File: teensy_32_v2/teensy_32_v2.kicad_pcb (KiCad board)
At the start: 2 copper layers, 65 x 56.5 mm, 62 parts, among them J1 277-1667-ND, J2 277-1667-ND, J3 CJ, J4 CJ, J5 CJ, J6 CJ, J7 M20-9980845, J8 M20-9970445, J9 TSW-108-07-G-T, P1 S9200-ND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

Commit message: more work on teensy shield
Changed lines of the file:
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@@
     (links 166)
     (no_connects 0)
-    (area 74.949999 59.949999 140.050001 116.550001)
+    (area 69.523819 58.652 146.962016 123.037092)
     (thickness 1.6)
     (drawings 87)
@@
   (page A4)
   (layers
-    (0 F.Cu signal hide)
+    (0 F.Cu signal)
     (31 B.Cu signal)
     (32 B.Adhes user hide)
@@
   )
   (setup
-    (last_trace_width 0.7)
+    (last_trace_width 1.2)
     (user_trace_width 0.25)
     (user_trace_width 0.45)
@@
     (pad_to_mask_clearance 0)
     (aux_axis_origin 0 0)
-    (visible_elements 7FFEBF7F)
+    (visible_elements 7FFEFF7F)
     (pcbplotparams
       (layerselection 0x010fc_80000001)
@@
   (segment (start 87.884 77.681) (end 86.319 77.681) (width 1.2) (layer F.Cu) (net 2))
   (segment (start 86.319 77.681) (end 84.2 79.8) (width 1.2) (layer F.Cu) (net 2))
-  (segment (start 107 96.8) (end 107 98.46) (width 0.7) (layer F.Cu) (net 2))
+  (segment (start 107 96.8) (end 107 98.46) (width 1.2) (layer F.Cu) (net 2))
   (segment (start 106.4 96.2) (end 107 96.8) (width 1.2) (layer F.Cu) (net 2))
   (segment (start 100 96.2) (end 106.4 96.2) (width 1.2) (layer F.Cu) (net 2))
@@
   (via (at 97 91.3) (size 0.465) (drill 0.31) (layers F.Cu B.Cu) (net 81))
   (segment (start 97.9395 90.3605) (end 97 91.3) (width 0.25) (layer B.Cu) (net 81))
-  (segment (start 107 103.54) (end 107 104.4) (width 1.8) (layer F.Cu) (net 81))
+  (segment (start 106.9 104.14) (end 106.9 105) (width 1.8) (layer F.Cu) (net 81))
   (segment (start 87.6935 96.0935) (end 87.6935 91.993) (width 1.2) (layer F.Cu) (net 81))
-  (segment (start 97.4 105.8) (end 87.6935 96.0935) (width 1.8) (layer F.Cu) (net 81))
-  (segment (start 105.6 105.8) (end 97.4 105.8) (width 1.8) (layer F.Cu) (net 81))
-  (segment (start 107 104.4) (end 105.6 105.8) (width 1.8) (layer F.Cu) (net 81))
-  (segment (start 107 103.54) (end 109.54 103.54) (width 0.7) (layer B.Cu) (net 81))
+  (segment (start 98 106.4) (end 87.6935 96.0935) (width 1.8) (layer F.Cu) (net 81))
+  (segment (start 105.5 106.4) (end 98 106.4) (width 1.8) (layer F.Cu) (net 81))
+  (segment (start 106.9 105) (end 105.5 106.4) (width 1.8) (layer F.Cu) (net 81))
+  (segment (start 107 103.54) (end 109.54 103.54) (width 1.2) (layer B.Cu) (net 81))
   (segment (start 109.47654 90.3605) (end 104.3 90.3605) (width 0.25) (layer B.Cu) (net 81))
   (segment (start 104.3 90.3605) (end 104.2395 90.3605) (width 0.25) (layer B.Cu) (net 81))

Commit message: teensy hat updates
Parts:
- added D10: SMCJ15A, Diodes_SMD:D_SMC_Standard, B.Cu at (81.1, 73.2)
- added J10: 0878980426, Pin_Headers:Pin_Header_Straight_1x04_Pitch2.54mm_SMD_Pin1Right, F.Cu at (80.9, 104.0)
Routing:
- net /Power/VIN: track 48.2 -> 65.6 mm, vias 2 -> 4
- net Net-(J10-Pad2): track 18.4 -> 28.7 mm, vias 0 -> 2
- net Net-(D9-Pad2): track 29.4 -> 34.4 mm, vias 2 -> 3
- net GND: track 317.6 -> 321.5 mm, vias 17 -> 18
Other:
- board text added: "11"
- board text added: "12"
- board text added: "2"
- board text added: "5"
- board text added: "6"
- board text removed: "14"
- board text removed: "15"
- board text removed: "4"
- board text removed: "7"
- board text removed: "8"

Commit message: Updates to hat for next manufacturing run (pre order)
remove unused directories

move over teensy3.lib library that was needed
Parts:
- added J11: Conn_01x04_Female, Pin_Headers:Pin_Header_Straight_1x04_Pitch2.54mm, F.Cu at (84.5, 59.1)
- added J12: Conn_01x08_Female, Pin_Headers:Pin_Header_Straight_1x08_Pitch2.54mm, F.Cu at (112.5, 59.1)
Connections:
- P1 pad 19: Net-(P1-Pad19) -> /R_MOSI
- P1 pad 21: Net-(P1-Pad21) -> /R_MISO
- P1 pad 22: Net-(P1-Pad22) -> /R_25
- P1 pad 23: Net-(P1-Pad23) -> /R_SCK
- P1 pad 24: Net-(P1-Pad24) -> /R_CE0
- P1 pad 26: Net-(P1-Pad26) -> /R_CE1
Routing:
- net +3V3: track 60.6 -> 81.8 mm, vias 3 -> 4
- net /R_SCK: track 0.00 -> 19.5 mm
- net /R_CE1: track 0.00 -> 17.8 mm
- net /R_MISO: track 0.00 -> 16.8 mm
- net /R_CE0: track 0.00 -> 15.2 mm
- net /R_MOSI: track 0.00 -> 14.8 mm
- net /R_25: track 0.00 -> 12.7 mm
- net /R_SDA: track 59.2 -> 67.9 mm
- net /R_SCL: track 56.7 -> 63.2 mm
- net /MSG_LED: track 5.78 -> 9.10 mm
- net GND: track 321.5 -> 323.9 mm
- net Net-(J10-Pad2): track 28.7 -> 28.8 mm, vias 2 -> 4
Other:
- board size 65 x 56.5 mm -> 65 x 59.5 mm
- board text added: "25"
- board text added: "3"
- board text added: "C"
- board text added: "D"
- board text added: "E0"
- board text added: "E1"
- board text added: "G"
- board text added: "I"
- board text added: "O"

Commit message: prep for order
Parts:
- J10: footprint Pin_Headers:Pin_Header_Straight_1x04_Pitch2.54mm_SMD_Pin1Right -> MF_Connectors:MF_Connectors-PTH_2.54MM_01X04
- moved J10 0.58 mm to (81.2, 103.5), turned to 0 degrees
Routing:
- net /Power/VIN: track 65.6 -> 57.3 mm
- net Net-(D9-Pad2): track 34.4 -> 36.2 mm, vias 3 -> 2
- net Net-(BT1-Pad1): track 24.9 -> 25.9 mm
- net GND: track 323.9 -> 323.2 mm, vias 18 -> 17
- net Net-(J10-Pad2): track 28.8 -> 28.2 mm, vias 4 -> 3
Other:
- board text added: "2018-01-22"
- board text added: "IMU"
- board text added: "SPI"
- board text added: "Teensy Hat for Donkey Car github.com/jwatte/donkey_racing 2018-02-22"
- board text removed: "2018-01-01"
- board text removed: "Teensy Hat for Donkey Car github.com/jwatte/donkey_racing 2018-01-01"

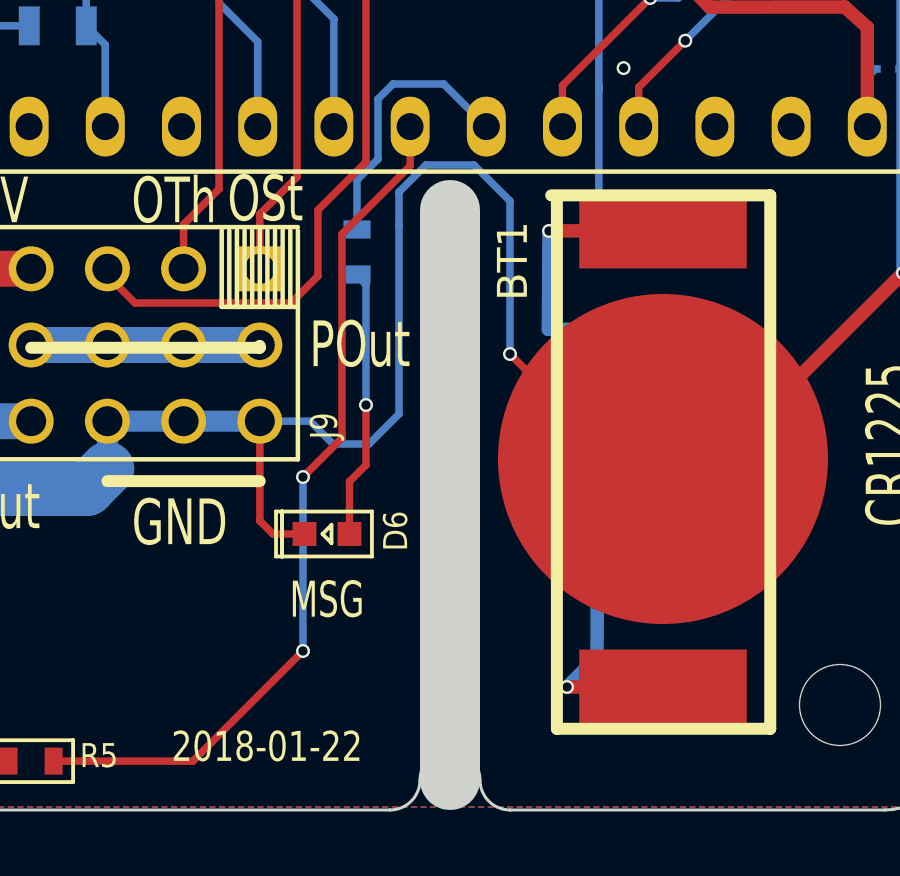
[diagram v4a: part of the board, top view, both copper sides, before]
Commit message: tweaks to TVS diodes and board outline slot
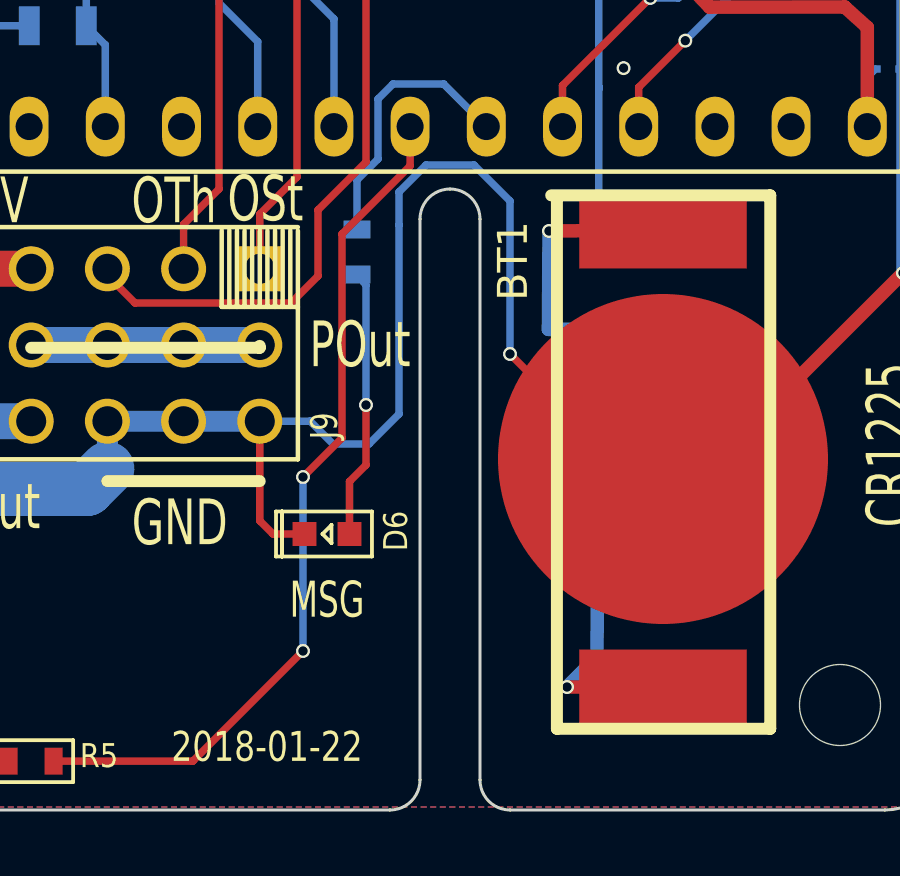
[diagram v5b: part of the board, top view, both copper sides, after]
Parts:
- D10: value SMCJ15A -> SMCJ16A
- D8: value SMAJ16A-E3/61 -> SMAJ15A-E3/61
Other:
- outline, holes or cut-outs redrawn
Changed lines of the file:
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@@
     (area 74.949999 56.949999 140.050001 116.550001)
     (thickness 1.6)
-    (drawings 108)
+    (drawings 109)
     (tracks 819)
     (zones 0)
@@
   )
   (setup
-    (last_trace_width 0.25)
+    (last_trace_width 0.13)
     (user_trace_width 0.25)
     (user_trace_width 0.45)
@@
       (drillshape 0)
       (scaleselection 1)
-      (outputdirectory macrofab_order_20171126))
+      (outputdirectory macrofab_order_20180222))
   )
   (net 0 "")
@@
       (effects (font (size 0.8 0.7) (thickness 0.175)) (justify mirror))
     )
-    (fp_text value SMAJ16A-E3/61 (at 0 -4.3) (layer B.Fab)
+    (fp_text value SMAJ15A-E3/61 (at 0 -4.3) (layer B.Fab)
       (effects (font (size 1 1) (thickness 0.15)) (justify mirror))
     )
@@
       (effects (font (size 1 0.8) (thickness 0.2)) (justify mirror))
     )
-    (fp_text value SMCJ15A (at 0 -5.08 180) (layer B.Fab)
+    (fp_text value SMCJ16A (at 0 -5.08 180) (layer B.Fab)
       (effects (font (size 1 1) (thickness 0.15)) (justify mirror))
     )
@@
       (net 70 /Power/VIN))
   )
+  (gr_line (start 122.5 115.5) (end 122.5 96.8) (angle 90) (layer Edge.Cuts) (width 0.1))
+  (gr_line (start 124.5 96.8) (end 124.5 115.5) (angle 90) (layer Edge.Cuts) (width 0.1))
   (gr_text SPI (at 133.4 59.1) (layer F.SilkS)
     (effects (font (size 1.2 1) (thickness 0.25)))
@@
   )
   (gr_arc (start 125.5 115.5) (end 125.5 116.5) (angle 90) (layer Edge.Cuts) (width 0.1))
-  (gr_arc (start 123.5 115.5) (end 123.5 114.5) (angle 90) (layer Edge.Cuts) (width 0.1))
-  (gr_arc (start 123.5 115.5) (end 122.5 115.5) (angle 90) (layer Edge.Cuts) (width 0.1))
+  (gr_arc (start 123.5 96.8) (end 123.5 95.8) (angle 90) (layer Edge.Cuts) (width 0.1))
+  (gr_arc (start 123.5 96.8) (end 122.5 96.8) (angle 90) (layer Edge.Cuts) (width 0.1))
   (gr_arc (start 121.5 115.5) (end 122.5 115.5) (angle 90) (layer Edge.Cuts) (width 0.1))
   (gr_line (start 121.5 116.5) (end 77 116.5) (angle 90) (layer Edge.Cuts) (width 0.1))
@@
     (effects (font (size 1.778 1.27) (thickness 0.3175)))
   )
-  (gr_line (start 123.5 96.5) (end 123.5 115.5) (angle 90) (layer Edge.Cuts) (width 2))
   (gr_arc (start 138 59) (end 138 57) (angle 90) (layer Edge.Cuts) (width 0.1))
   (gr_arc (start 138 114.5) (end 140 114.5) (angle 90) (layer Edge.Cuts) (width 0.1))
@@
   (via (at 126.8 97.2) (size 0.465) (drill 0.31) (layers F.Cu B.Cu) (net 73))
   (segment (start 126.8 97.2) (end 126.77986 100.47986) (width 0.45) (layer B.Cu) (net 73))
-  (segment (start 126.77986 100.47986) (end 128.4605 100.47986) (width 0.45) (layer B.Cu) (net 73) (status 800000))
+  (segment (start 126.77986 100.47986) (end 128.4605 100.47986) (width 0.45) (layer B.Cu) (net 73))
   (segment (start 104.3 90.3605) (end 97.9395 90.3605) (width 0.25) (layer B.Cu) (net 74))
   (segment (start 96.7 91.6) (end 93.6 91.6) (width 0.25) (layer F.Cu) (net 74))
